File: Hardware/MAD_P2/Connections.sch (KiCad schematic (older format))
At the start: 48 parts, among them J10 Conn_02x05_Odd_Even, J11 Conn_02x05_Odd_Even, J13 Conn_02x05_Odd_Even, J14 Conn_02x05_Odd_Even, J15 Conn_ADC1, J16 Conn_DAC, J18 P3, J19 P4, J20 P2, J21 Conn_02x05_Odd_Even, J22 Conn_02x05_Odd_Even, J23 Conn_02x03_Odd_Even, J24 P5, J25 P6, J26 P7, J31 Micro_SD_Card_Connector, J32 Micro_SD_Card_Socket, J6 Edge_Conn, J7 Conn_02x05_Odd_Even, J8 USB_C_Receptacle_USB2.0, J9 Conn_02x05_Odd_Even, Q1 MMBT3904, U27 FT232RL

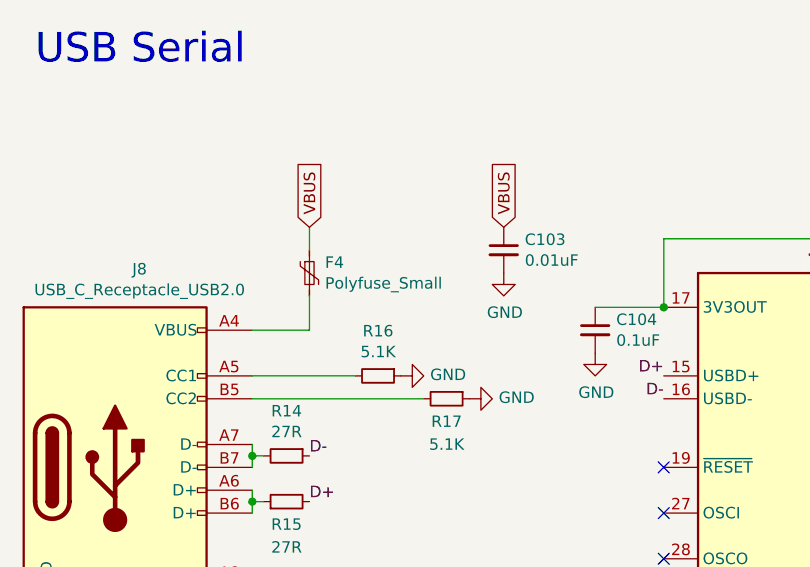
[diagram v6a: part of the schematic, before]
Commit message: completed BOM with digikey and LSCS parts
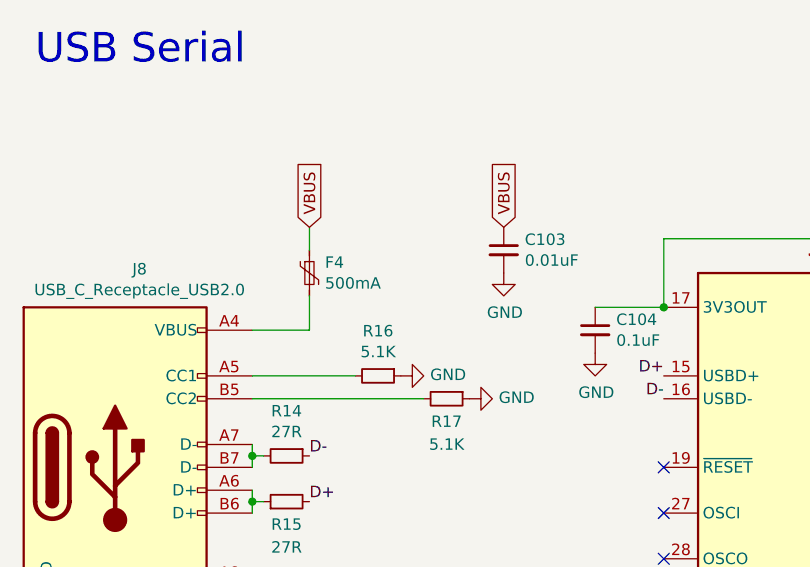
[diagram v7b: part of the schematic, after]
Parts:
- C103, C107: LCSC (none) -> C57112; TYPE (none) -> BASIC
- C104, C105: LCSC (none) -> C14663; TYPE (none) -> BASIC
- C106: footprint Capacitor_SMD:C_0603_1608Metric -> Capacitor_SMD:C_0805_2012Metric; LCSC (none) -> C15850; TYPE (none) -> BASIC
- D12: LCSC (none) -> C72043; TYPE (none) -> BASIC
- D9: LCSC (none) -> C72041; TYPE (none) -> BASIC
- F4: value Polyfuse_Small -> 500mA; LCSC (none) -> C261937; TYPE (none) -> EXT
- J10, J11, J13, J14, J21, J22, J6, J7, J9, JP13, JP14, JP15, JP16, JP17: TYPE (none) -> NA
- J15, J16: DIGIKEY (none) -> S9169-ND; TYPE (none) -> DIGIKEY
- J18, J19, J20, J23, J24, J25, J26: TYPE (none) -> AMAZON
- J31: DIGIKEY (none) -> WM26501; TYPE (none) -> DIGIKEY
- J32: DIGIKEY (none) -> 732-3820-2-ND; TYPE (none) -> DIGIKEY
- J8: LCSC (none) -> C165948; TYPE (none) -> EXT
- Q1: LCSC (none) -> C20526; TYPE (none) -> BASIC
- R1, R20: LCSC (none) -> C25804; TYPE (none) -> BASIC
- R14, R15: LCSC (none) -> C25190; TYPE (none) -> BASIC
- R16, R17: LCSC (none) -> C23186; TYPE (none) -> BASIC
- R18, R19, R35, R36: LCSC (none) -> C23350; TYPE (none) -> BASIC
- R21, R22: LCSC (none) -> C21190; TYPE (none) -> BASIC
- U27: LCSC (none) -> C8690; TYPE (none) -> BASIC

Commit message: Finished re-routing the power and important connections. exported dsn for this stage of routing. running autorouter, may have few more commits before finished route
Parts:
- added J34: FTDI 1x6, Connector_PinHeader_2.54mm:PinHeader_1x06_P2.54mm_Vertical, symbol Connector_Generic:Conn_01x06
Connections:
- net GND: now also J11.1 (Pin_1), J34.6 (Pin_6)
- net P62: now also J34.2 (Pin_2)
- net P63: now also J34.3 (Pin_3)
- net RESET: now also J34.1 (Pin_1)
- net VBUS: now also J34.4 (Pin_4)
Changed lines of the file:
@@
 Text GLabel 4800 7450 3    50   Input ~ 0
 V_48_51
-NoConn ~ 4600 7450
 Text GLabel 5100 4750 1    50   Input ~ 0
 P34
@@
 Wire Wire Line
 	10000 1650 10000 1800
+$Comp
+L Connector_Generic:Conn_01x06 J34
+U 1 1 60E2D1E3
+P 4600 3050
+F 0 "J34" H 4680 3042 50  0000 L CNN
+F 1 "FTDI 1x6" H 4680 2951 50  0000 L CNN
+F 2 "Connector_PinHeader_2.54mm:PinHeader_1x06_P2.54mm_Vertical" H 4600 3050 50  0001 C CNN
+F 3 "~" H 4600 3050 50  0001 C CNN
+	1    4600 3050
+	1    0    0    -1
+$EndComp
+Text GLabel 4400 2850 0    50   Input ~ 0
+RESET
+Text GLabel 4400 2950 0    50   Input ~ 0
+P62
+Text GLabel 4400 3050 0    50   Input ~ 0
+P63
+Text GLabel 4400 3150 0    50   Input ~ 0
+VBUS
+NoConn ~ 4400 3250
+$Comp
+L power:GND #PWR?
+U 1 1 60E38545
+P 4400 3350
+AR Path="/60B76FA1/60E38545" Ref="#PWR?"  Part="1"
+AR Path="/60BD9EA1/60E38545" Ref="#PWR0257"  Part="1"
+F 0 "#PWR0257" H 4400 3100 50  0001 C CNN
+F 1 "GND" V 4405 3222 50  0000 R CNN
+F 2 "" H 4400 3350 50  0001 C CNN
+F 3 "" H 4400 3350 50  0001 C CNN
+	1    4400 3350
+	0    1    1    0
+$EndComp
+$Comp
+L power:GND #PWR0258
+U 1 1 60E47354
+P 4600 7450
+F 0 "#PWR0258" H 4600 7200 50  0001 C CNN
+F 1 "GND" H 4605 7277 50  0000 C CNN
+F 2 "" H 4600 7450 50  0001 C CNN
+F 3 "" H 4600 7450 50  0001 C CNN
+	1    4600 7450
+	0    1    1    0
+$EndComp
 $EndSCHEMATC
